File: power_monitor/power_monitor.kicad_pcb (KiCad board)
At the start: 2 copper layers, 4 parts, among them J1 BATT, J2 VEH, U1 ACS712ELCTR-20A, X1 ATmega328-A

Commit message: Touched up schematic and initial layout
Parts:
- removed X1: ATmega328-A, Package_QFP:TQFP-32_7x7mm_P0.8mm
- added C1: 10 nF, Capacitor_SMD:C_0603_1608Metric, F.Cu at (57.0, 90.5)
- added C10: 10uF, Capacitor_SMD:C_0805_2012Metric, F.Cu at (105.0, 96.9)
- added C11: 1 uF, Capacitor_SMD:C_0603_1608Metric, F.Cu at (130.8, 134.3)
- added C12: 10uF, Capacitor_SMD:C_0805_2012Metric, F.Cu at (140.4, 58.8)
- added C13: 22uF, Capacitor_SMD:C_0805_2012Metric, F.Cu at (140.2, 63.8)
- added C14: 22 uF, Capacitor_SMD:C_0805_2012Metric, F.Cu at (134.3, 134.6)
- added C2: 100 nF, Capacitor_SMD:C_0603_1608Metric, F.Cu at (57.2, 94.5)
- added C3: 1 nF, Capacitor_SMD:C_0603_1608Metric, F.Cu at (96.2, 63.0)
- added C4: 100 nF, Capacitor_SMD:C_0603_1608Metric, F.Cu at (101.2, 61.8)
- added C5: 0.1uF, Capacitor_SMD:C_0603_1608Metric, F.Cu at (110.3, 96.5)
- added C6: 10uF, Capacitor_SMD:C_0805_2012Metric, F.Cu at (110.5, 91.8)
- added C7: 0.1uF, Capacitor_SMD:C_0603_1608Metric, F.Cu at (110.2, 100.8)
- added C8: 0.1uF, Capacitor_SMD:C_0603_1608Metric, F.Cu at (102.5, 96.9)
- added C9: 10uF, Capacitor_SMD:C_0805_2012Metric, F.Cu at (110.2, 105.0)
- added J3: Conn_01x04_Socket, Connector_JST:JST_XA_B04B-XASK-1_1x04_P2.50mm_Vertical, F.Cu at (68.0, 128.5)
- added J4: BATT, Connector_AMASS:AMASS_XT60-M_1x02_P7.20mm_Vertical, F.Cu at (112.0, 62.6)
- added J5: VEH, Connector_AMASS:AMASS_XT60-F_1x02_P7.20mm_Vertical, F.Cu at (83.0, 62.9)
- added JP1: Power Connect, Jumper:SolderJumper-2_P1.3mm_Open_Pad1.0x1.5mm, F.Cu at (67.7, 137.9)
- added R1: 10k, Resistor_SMD:R_0603_1608Metric, F.Cu at (29.0, 100.3)
- added R2: 10k, Resistor_SMD:R_0603_1608Metric, F.Cu at (59.8, 103.5)
- added R3: 30k, Resistor_SMD:R_0603_1608Metric, F.Cu at (97.4, 101.2)
- added R4: 10k, Resistor_SMD:R_0603_1608Metric, F.Cu at (97.5, 96.8)
- added S1: RST, Button_Switch_SMD:SW_SPST_SKQG_WithStem, F.Cu at (35.2, 102.2)
- added U2: ACS712ELCTR-20A, Package_SO:SOIC-8_3.9x4.9mm_P1.27mm, F.Cu at (97.6, 58.2)
- added U3: ~, ADC Pretty:QFN-12_EP_2x2_Pitch0.4mm, F.Cu at (103.3, 101.3)
- added U4: AZ1117-3.3, Package_TO_SOT_SMD:SOT-223-3_TabPin2, F.Cu at (147.5, 61.5)
- added U5: TS2940CW50, Package_TO_SOT_SMD:SOT-223-3_TabPin2, F.Cu at (132.5, 129.0)
- added Y1: 8M, Crystal:Resonator_SMD_Murata_CSTxExxV-3Pin_3.0x1.1mm, F.Cu at (55.5, 100.5)
- J1: value BATT -> AVR-ISP-6; footprint Connector_AMASS:AMASS_XT60-F_1x02_P7.20mm_Vertical -> Connector_PinHeader_2.54mm:PinHeader_2x03_P2.54mm_Vertical_SMD
- J2: value VEH -> Conn_01x06_Female; footprint Connector_AMASS:AMASS_XT60-M_1x02_P7.20mm_Vertical -> Connector_PinHeader_2.54mm:PinHeader_1x06_P2.54mm_Vertical
- U1: value ACS712ELCTR-20A -> ATmega328-A; footprint Package_SO:SOIC-8_3.9x4.9mm_P1.27mm -> Package_QFP:TQFP-32_7x7mm_P0.8mm
- moved U1 107.2 mm to (47.5, 102.7), turned to 180 degrees
- moved J2 100.1 mm to (40.9, 114.8), turned to 90 degrees
- moved J1 87.4 mm to (47.0, 80.3)
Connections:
- J1 pad 1: GND -> MISO
- J1 pad 2: BATT -> +5V
- J2 pad 2: VEH -> unconnected-(J2-Pin_2-Pad2)
- U1 pad 1: BATT -> unconnected-(U1-PD3-Pad1)
- U1 pad 2: BATT -> unconnected-(U1-PD4-Pad2)
- U1 pad 3: VEH -> GND
- U1 pad 4: VEH -> +3V3
- U1 pad 6: Net-(U1-FILTER) -> +3V3
- U1 pad 8: 5V_reg -> Net-(U1-XTAL2/PB7)

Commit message: Added symbol library
yes
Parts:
- moved C11 40.1 mm to (127.1, 94.4)
- moved C14 40.1 mm to (130.6, 94.7)
- moved U5 40.1 mm to (128.8, 89.1)
- moved R3 29.8 mm to (118.7, 80.5), turned to 180 degrees
- moved C9 27.9 mm to (107.3, 77.2), turned to 180 degrees
- moved C12 26.9 mm to (140.2, 85.7), turned to 90 degrees
- moved R4 24.4 mm to (118.7, 84.8), turned to 0 degrees
- moved U3 22.9 mm to (112.8, 80.4), turned to 90 degrees
- moved U4 22.1 mm to (146.0, 83.5)
- moved C7 19.5 mm to (107.2, 81.5), turned to 180 degrees
- moved C13 18.4 mm to (140.2, 82.1), turned to 90 degrees
- moved C8 17.3 mm to (114.0, 84.0), turned to -90 degrees
- moved C10 14.6 mm to (112.0, 84.1), turned to -90 degrees
- moved C5 11.2 mm to (107.1, 85.8), turned to 180 degrees
- moved C6 3.77 mm to (107.0, 90.4), turned to 180 degrees
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
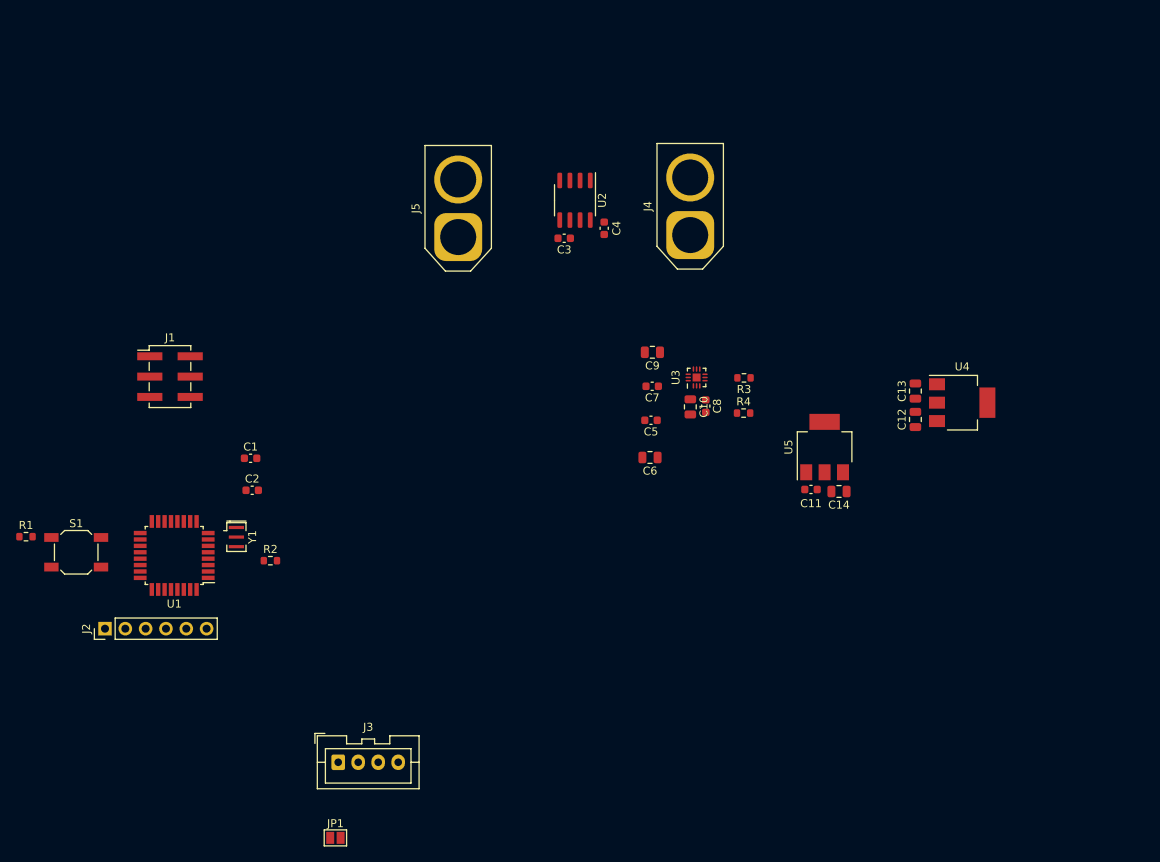
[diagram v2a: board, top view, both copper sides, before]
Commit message: PCB Layout
Created initial PCB layout and included more complicated connections to give an idea of what's going on. There's a connection that goes under the board since my brain does not know how to rearrange the components to work all on the front. Also, I made a board outline :D. Also this made me a bit crazy
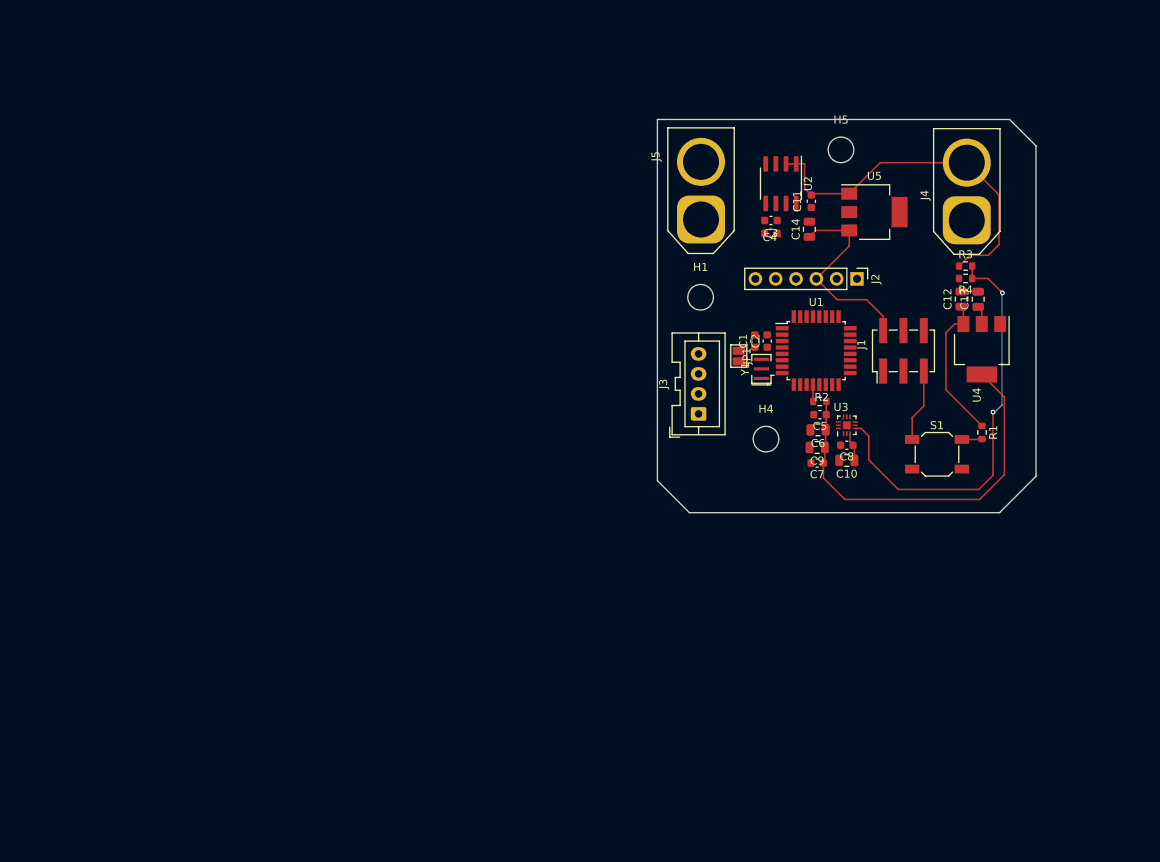
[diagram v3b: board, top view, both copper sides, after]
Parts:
- added H1: MountingHole, MountingHole:MountingHole_3.2mm_M3_ISO14580, F.Cu at (113.3, 70.4)
- added H4: MountingHole, MountingHole:MountingHole_3.2mm_M3_ISO14580, F.Cu at (121.5, 88.1)
- added H5: MountingHole, MountingHole:MountingHole_3.2mm_M3_ISO14580, F.Cu at (130.8, 52.0)
- moved R1 120.2 mm to (148.5, 87.3), turned to -90 degrees
- moved S1 108.3 mm to (142.8, 90.0)
- moved J2 103.7 mm to (132.8, 68.1), turned to -90 degrees
- moved J1 91.7 mm to (138.7, 77.1), turned to 90 degrees
- moved U1 84.2 mm to (127.8, 77.0), turned to 0 degrees
- moved JP1 78.5 mm to (118.1, 77.7), turned to -90 degrees
- moved R2 71.5 mm to (128.2, 83.4)
- moved Y1 68.9 mm to (120.9, 79.3), turned to 90 degrees
- moved C2 67.0 mm to (121.6, 75.8), turned to 90 degrees
- moved C1 64.7 mm to (120.1, 75.8), turned to 90 degrees
- moved J3 62.7 mm to (113.0, 85.0), turned to 90 degrees
- moved C11 36.0 mm to (127.1, 58.4), turned to -90 degrees
- moved J4 34.6 mm to (146.6, 60.8)
- moved C14 33.0 mm to (126.9, 61.9), turned to 90 degrees
- moved R4 32.5 mm to (146.4, 68.0), turned to 180 degrees
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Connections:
- JP1 pad 1: +5V -> +3V3
- U1 pad 14: SS -> unconnected-(U1-PB2-Pad14)
- U3 pad 13: (no net) -> GND
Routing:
- net /BATT_DIVIDED: track 0.00 -> 52.4 mm, vias 0 -> 2
- net +3V3: track 0.00 -> 51.6 mm
- net +BATT: track 0.00 -> 46.0 mm
- net +5V: track 0.00 -> 44.2 mm
- net RESET: track 0.00 -> 11.7 mm
- net Net-(U3-REFIN+): track 0.00 -> 3.58 mm
- net CS: track 0.00 -> 2.11 mm
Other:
- board outline added: 47.3 x 49.1 mm

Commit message: PCB Layout finished
HAHAHAHAHA IT'S DONE. will commence routing.
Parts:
- added H2: MountingHole, MountingHole:MountingHole_3.2mm_M3_ISO14580, F.Cu at (90.0, 81.0)
- moved C13 61.7 mm to (95.3, 38.6)
- moved U4 60.2 mm to (101.0, 39.8), turned to 0 degrees
- moved C12 58.4 mm to (94.7, 42.4), turned to 180 degrees
- moved J1 40.7 mm to (101.5, 60.5), turned to 180 degrees
- moved H1 38.3 mm to (90.0, 40.0)
- moved J2 37.0 mm to (98.8, 82.5), turned to 90 degrees
- moved R3 37.0 mm to (113.5, 49.7), turned to -90 degrees
- moved R4 36.3 mm to (113.5, 52.7), turned to -90 degrees
- moved C10 35.2 mm to (114.5, 60.0), turned to -90 degrees
- moved C8 34.6 mm to (112.6, 60.0), turned to -90 degrees
- moved U3 34.0 mm to (110.1, 60.0), turned to 180 degrees
- moved U5 31.7 mm to (110.3, 39.8), turned to 180 degrees
- moved R1 31.6 mm to (123.0, 68.5)
- moved S1 31.2 mm to (117.9, 71.3)
- moved J3 31.0 mm to (90.5, 63.8), turned to -90 degrees
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- renumbered H5 to H3
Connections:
- J1 pad 2: +5V -> +3V3
- J2 pad 3: +5V -> +3V3
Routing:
- net /BATT_DIVIDED: track 52.4 -> 0.00 mm, vias 2 -> 0
- net +3V3: track 51.6 -> 0.00 mm
- net +BATT: track 46.0 -> 0.00 mm
- net +5V: track 44.2 -> 0.00 mm
- net RESET: track 11.7 -> 0.00 mm
- net Net-(U3-REFIN+): track 3.58 -> 0.00 mm
- net CS: track 2.11 -> 0.00 mm
- net MISO: track 0.00 -> 1.08 mm
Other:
- board outline removed

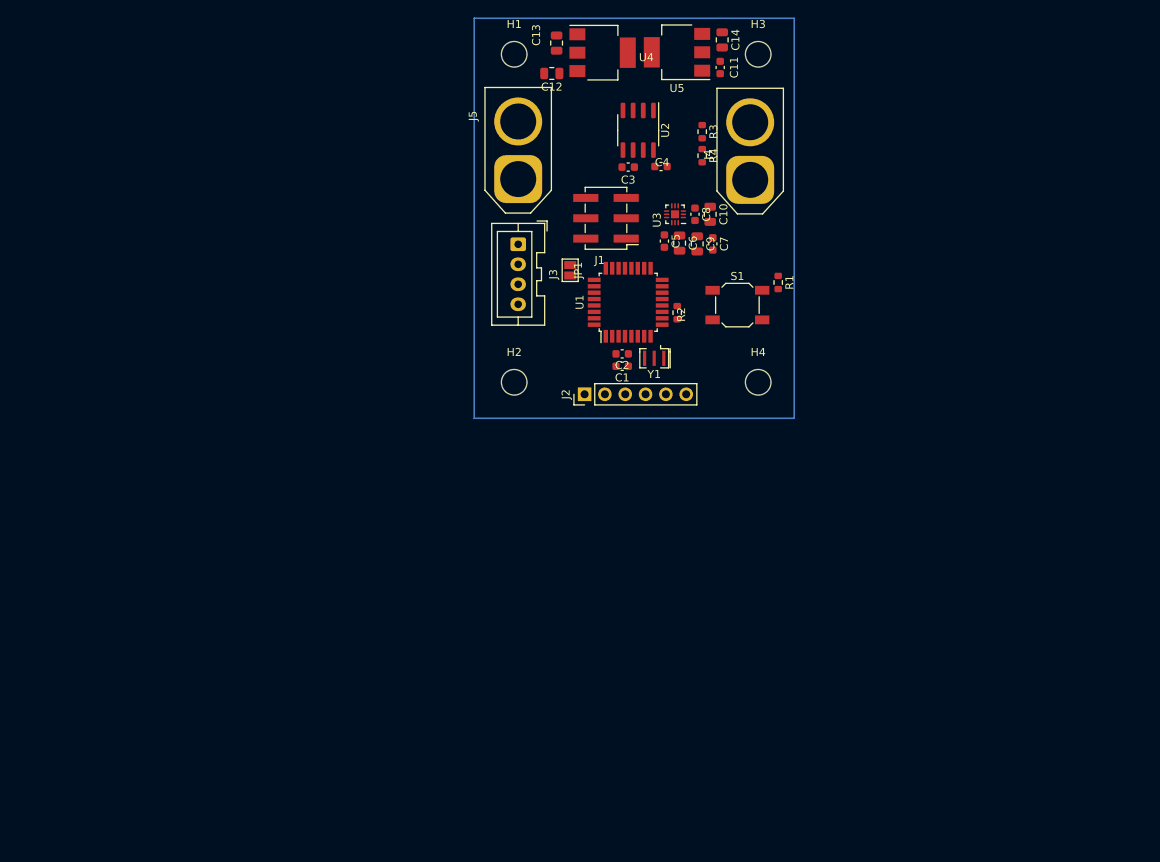
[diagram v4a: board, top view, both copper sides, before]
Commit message: Preliminary routing
Rough ideas for routing. Didn't do any ground connections yet.
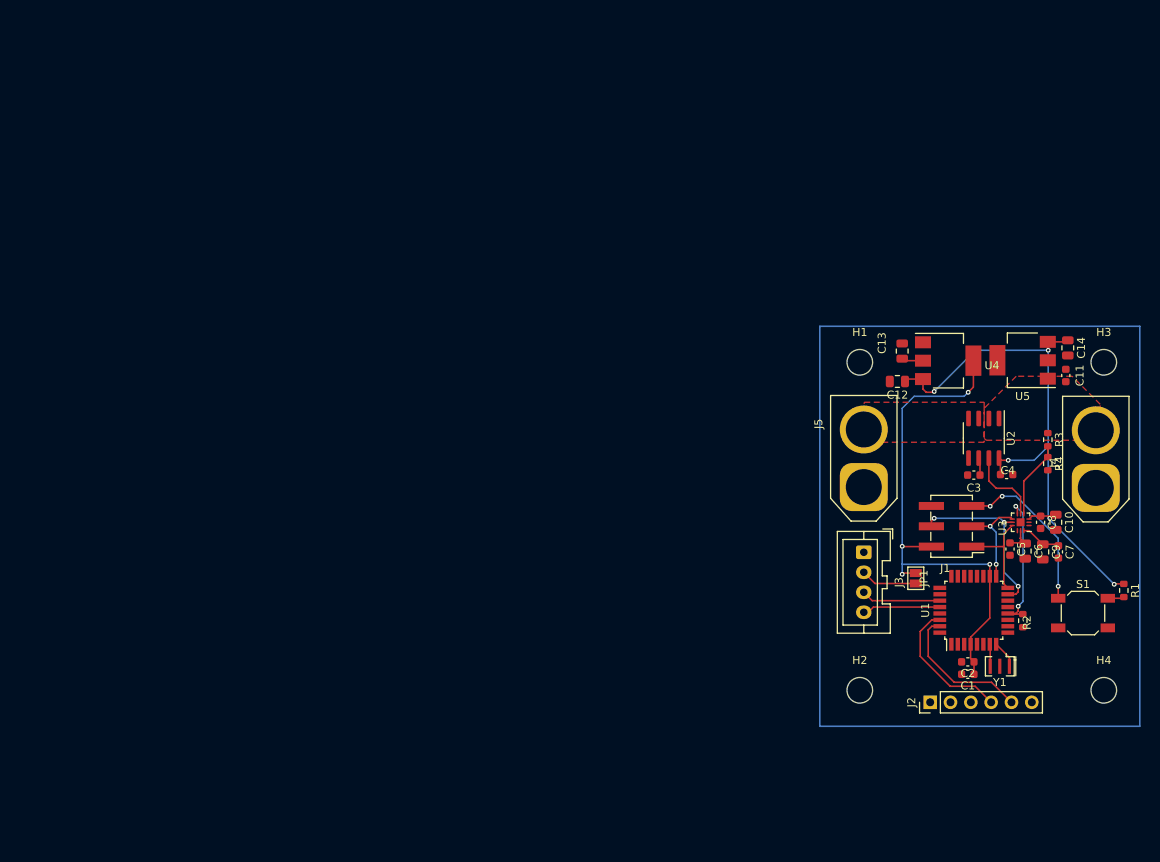
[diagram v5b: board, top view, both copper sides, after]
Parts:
- moved C8 57.9 mm to (155.8, 98.5)
- moved J1 57.9 mm to (144.7, 99.0)
- moved U3 57.9 mm to (153.3, 98.5)
- moved U5 57.9 mm to (153.6, 78.2)
- moved C12 57.9 mm to (137.9, 80.9)
- moved C11 57.9 mm to (158.9, 80.2)
- moved C13 57.9 mm to (138.5, 77.1)
- moved C4 57.9 mm to (151.6, 92.5)
- moved C6 57.9 mm to (153.9, 102.1)
- moved C7 57.9 mm to (158.0, 102.2)
- moved J2 57.9 mm to (142.0, 121.0)
- moved U4 57.9 mm to (144.2, 78.3)
- moved C1 57.9 mm to (146.7, 117.5)
- moved C10 57.9 mm to (157.7, 98.5)
- moved C14 57.9 mm to (159.2, 76.7)
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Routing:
- net +3V3: track 0.00 -> 77.1 mm, vias 0 -> 4
- net +5V: track 0.00 -> 68.3 mm, vias 0 -> 4
- net RESET: track 0.00 -> 23.1 mm, vias 0 -> 3
- net MOSI: track 0.05 -> 22.0 mm, vias 0 -> 3
- net CS: track 0.00 -> 18.1 mm, vias 0 -> 2
- net TXD: track 0.00 -> 17.7 mm
- net RXD: track 0.00 -> 17.4 mm
- net SCK: track 0.00 -> 12.1 mm, vias 0 -> 2
- net MISO: track 1.08 -> 12.5 mm
- net SDA: track 0.00 -> 9.93 mm
- net /CURRENT: track 0.00 -> 9.79 mm
- net SCL: track 0.00 -> 9.77 mm
- net /BATT_DIVIDED: track 0.00 -> 9.69 mm
- net Net-(J3-Pin_2): track 0.00 -> 7.08 mm
- net Net-(U3-REFIN+): track 0.00 -> 3.58 mm
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- added copper zone on F.Cu, net (none)
- added copper zone on F.Cu, net VEH

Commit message: haHA
Routing :D
Silkscreen :\
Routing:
- net +3V3: track 77.1 -> 18.8 mm, vias 4 -> 11
- net RESET: track 23.1 -> 46.5 mm
- net +5V: track 68.3 -> 83.1 mm, vias 4 -> 2
- net /BATT_DIVIDED: track 9.69 -> 13.4 mm
- net CS: track 18.1 -> 18.6 mm
- added copper zone on B.Cu, net +3V3
- added copper zone on F.Cu, net +BATT
- added copper zone on B.Cu, net GND
- added copper zone on F.Cu, net GND
- removed copper zone on F.Cu, net (none)
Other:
- board outline added: 40 x 50 mm
